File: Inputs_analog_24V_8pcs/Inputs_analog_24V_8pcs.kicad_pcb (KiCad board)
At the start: 2 copper layers, 102 parts, among them J1 Screw_Terminal_01x02, J10 Screw_Terminal_01x03, J11 Screw_Terminal_01x03, J2 Screw_Terminal_01x02, J3 Screw_Terminal_01x06, J4 Screw_Terminal_01x03, J5 Screw_Terminal_01x03, J6 Screw_Terminal_01x03, J7 Screw_Terminal_01x03, J8 Screw_Terminal_01x03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

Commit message: Update pcb
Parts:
- moved J3 132.5 mm to (152.4, 58.4), turned to 0 degrees
- moved C2 99.1 mm to (50.8, 66.0), turned to 90 degrees
- moved U3 96.8 mm to (120.7, 74.9), turned to 90 degrees
- moved U2 93.8 mm to (55.9, 67.3), turned to 90 degrees
- moved C3 89.6 mm to (116.8, 73.7), turned to 90 degrees
- moved U1 86.4 mm to (27.9, 67.3), turned to 90 degrees
- moved C1 81.5 mm to (22.9, 66.0), turned to 90 degrees
- moved C11 17.8 mm to (130.8, 121.9)
- moved C12 17.8 mm to (102.9, 121.9)
- moved C14 17.8 mm to (139.6, 96.5)
- moved C15 17.8 mm to (111.7, 96.5)
- moved C16 17.8 mm to (74.9, 121.9)
- moved C17 17.8 mm to (47.0, 121.9)
- moved C18 17.8 mm to (55.8, 96.5)
- moved C19 17.8 mm to (83.8, 96.5)
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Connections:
- U1 pad 1: input_1 -> Net-(U1-Pad1)
- U1 pad 10: GND -> Net-(U1-Pad10)
- U1 pad 11: GND -> Net-(U1-Pad11)
- U1 pad 12: GND -> Net-(U1-Pad12)
- U1 pad 13: GND -> Net-(U1-Pad13)
- U1 pad 3: input_2 -> Net-(U1-Pad3)
- U1 pad 5: input_3 -> Net-(U1-Pad5)
- U1 pad 9: input_4 -> Net-(U1-Pad9)
- U2 pad 1: input_5 -> Net-(U2-Pad1)
- U2 pad 10: GND -> Net-(U2-Pad10)
- U2 pad 11: GND -> Net-(U2-Pad11)
- U2 pad 12: GND -> Net-(U2-Pad12)
- U2 pad 13: GND -> Net-(U2-Pad13)
- U2 pad 3: input_6 -> Net-(U2-Pad3)
- U2 pad 5: input_7 -> Net-(U2-Pad5)
- U2 pad 9: input_8 -> Net-(U2-Pad9)
- U3 pad 1: Net-(U1-Pad8) -> Net-(U3-Pad1)
- U3 pad 12: Net-(U2-Pad8) -> Net-(U3-Pad12)
- U3 pad 13: Net-(U2-Pad6) -> Net-(U3-Pad13)
- U3 pad 14: Net-(U2-Pad4) -> Net-(U3-Pad14)
- U3 pad 15: Net-(U2-Pad2) -> Net-(U3-Pad15)
- U3 pad 2: Net-(U1-Pad6) -> Net-(U3-Pad2)
- U3 pad 3: Net-(U1-Pad4) -> Net-(U3-Pad3)
- U3 pad 4: Net-(U1-Pad2) -> Net-(U3-Pad4)
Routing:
- net +5V: track 490.0 -> 592.1 mm
- net GND: track 595.3 -> 671.4 mm
- net Earth: track 725.7 -> 743.5 mm
- net +24V: track 346.3 -> 364.1 mm

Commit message: Update pcb
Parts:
- added R52: 0, Resistor_THT:R_Axial_DIN0207_L6.3mm_D2.5mm_P7.62mm_Horizontal, F.Cu at (40.6, 88.9)
- added R53: 0, Resistor_THT:R_Axial_DIN0207_L6.3mm_D2.5mm_P7.62mm_Horizontal, F.Cu at (40.6, 92.7)
- moved C3 66.5 mm to (182.9, 66.0)
- moved C2 47.9 mm to (95.2, 83.8)
- moved U2 46.7 mm to (99.1, 85.1)
- moved C1 24.3 mm to (39.4, 83.8)
- moved R11 23.4 mm to (132.1, 40.6)
- moved R35 23.4 mm to (142.2, 111.8)
- moved R50 23.4 mm to (66.0, 116.8)
- moved C14 23.4 mm to (157.4, 111.8)
- moved C15 23.4 mm to (129.5, 111.8)
- moved C18 23.4 mm to (73.6, 111.8)
- moved C19 23.4 mm to (101.6, 111.8)
- moved R15 23.4 mm to (128.3, 48.3)
- moved R28 23.4 mm to (132.1, 129.5)
- moved R3 23.4 mm to (40.6, 125.7)
- moved R32 23.4 mm to (128.3, 129.5)
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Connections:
- U1 pad 1: Net-(U1-Pad1) -> input_7
- U1 pad 11: Net-(U1-Pad11) -> input_2
- U1 pad 13: Net-(U1-Pad13) -> input_1
- U1 pad 3: Net-(U1-Pad3) -> Net-(R52-Pad2)
- U1 pad 4: Net-(U1-Pad4) -> Net-(R52-Pad2)
- U1 pad 5: Net-(U1-Pad5) -> Net-(R52-Pad2)
- U1 pad 6: Net-(U1-Pad6) -> Net-(R52-Pad2)
- U1 pad 7: GND -> Net-(R53-Pad2)
- U1 pad 9: Net-(U1-Pad9) -> input_3
- U2 pad 1: Net-(U2-Pad1) -> input_8
- U2 pad 10: Net-(U2-Pad10) -> GND
- U2 pad 11: Net-(U2-Pad11) -> GND
- U2 pad 12: Net-(U2-Pad12) -> GND
- U2 pad 13: Net-(U2-Pad13) -> GND
- U2 pad 3: Net-(U2-Pad3) -> input_6
- U2 pad 5: Net-(U2-Pad5) -> input_5
- U2 pad 9: Net-(U2-Pad9) -> input_4
- U3 pad 1: Net-(U3-Pad1) -> Net-(U1-Pad8)
- U3 pad 14: Net-(U3-Pad14) -> Net-(U1-Pad12)
- U3 pad 15: Net-(U3-Pad15) -> Net-(U1-Pad10)
- U3 pad 4: Net-(U3-Pad4) -> Net-(U1-Pad2)
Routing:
- net input_3: track 14.4 -> 80.3 mm
- net input_5: track 14.4 -> 80.2 mm
- net +5V: track 592.1 -> 527.8 mm
- net input_4: track 28.3 -> 86.8 mm
- net input_7: track 14.4 -> 60.9 mm
- net input_2: track 14.4 -> 58.2 mm
- net input_6: track 14.4 -> 57.3 mm
- net input_8: track 14.3 -> 43.1 mm
- net input_1: track 14.4 -> 37.5 mm
- net Net-(U1-Pad2): track 0.00 -> 20.8 mm
- net Net-(U1-Pad12): track 0.00 -> 19.6 mm
- net Net-(R52-Pad2): track 0.00 -> 18.3 mm
- net Net-(J3-Pad4): track 0.00 -> 16.8 mm
- net Net-(R53-Pad2): track 0.00 -> 15.5 mm
- net Net-(J3-Pad1): track 0.00 -> 14.3 mm
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
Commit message: Finish pcb
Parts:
- added R54: 0, Resistor_THT:R_Axial_DIN0207_L6.3mm_D2.5mm_P7.62mm_Horizontal, F.Cu at (109.2, 86.4)
- added R55: 0, Resistor_THT:R_Axial_DIN0207_L6.3mm_D2.5mm_P7.62mm_Horizontal, F.Cu at (104.1, 86.4)
- added R56: 0, Resistor_THT:R_Axial_DIN0207_L6.3mm_D2.5mm_P7.62mm_Horizontal, F.Cu at (99.1, 86.4)
- added R57: 0, Resistor_THT:R_Axial_DIN0207_L6.3mm_D2.5mm_P7.62mm_Horizontal, F.Cu at (127.0, 85.1)
- added R58: 0, Resistor_THT:R_Axial_DIN0207_L6.3mm_D2.5mm_P7.62mm_Horizontal, F.Cu at (130.8, 94.0)
- added R59: 0, Resistor_THT:R_Axial_DIN0207_L6.3mm_D2.5mm_P7.62mm_Horizontal, F.Cu at (167.6, 94.0)
- added R60: 0, Resistor_THT:R_Axial_DIN0207_L6.3mm_D2.5mm_P7.62mm_Horizontal, F.Cu at (123.2, 94.0)
- added R61: 0, Resistor_THT:R_Axial_DIN0207_L6.3mm_D2.5mm_P7.62mm_Horizontal, F.Cu at (119.4, 94.0)
- added R62: 0, Resistor_THT:R_Axial_DIN0207_L6.3mm_D2.5mm_P7.62mm_Horizontal, F.Cu at (152.4, 88.3)
- added R63: 0, Resistor_THT:R_Axial_DIN0207_L6.3mm_D2.5mm_P7.62mm_Horizontal, F.Cu at (92.1, 69.8)
- added R64: 0, Resistor_THT:R_Axial_DIN0207_L6.3mm_D2.5mm_P7.62mm_Horizontal, F.Cu at (86.4, 69.8)
- added R65: 0, Resistor_THT:R_Axial_DIN0207_L6.3mm_D2.5mm_P7.62mm_Horizontal, F.Cu at (114.3, 94.0)
- added R66: 0, Resistor_THT:R_Axial_DIN0207_L6.3mm_D2.5mm_P7.62mm_Horizontal, F.Cu at (95.2, 86.4)
- added R67: 0, Resistor_THT:R_Axial_DIN0207_L6.3mm_D2.5mm_P7.62mm_Horizontal, F.Cu at (100.3, 97.2)
- moved C3 54.6 mm to (130.8, 82.5)
- moved C11 3.81 mm to (148.6, 133.3)
- moved C12 3.81 mm to (120.7, 133.3)
- moved C14 3.81 mm to (157.4, 108.0)
- moved C15 3.81 mm to (129.5, 108.0)
- moved C16 3.81 mm to (92.7, 133.3)
- moved C17 3.81 mm to (64.8, 133.3)
- moved C18 3.81 mm to (73.6, 108.0)
- moved C19 3.81 mm to (101.6, 108.0)
- moved J10 3.81 mm to (61.0, 133.3)
- moved J11 3.81 mm to (88.9, 133.3)
- moved J2 3.81 mm to (40.6, 133.3)
- moved J8 3.81 mm to (144.8, 133.3)
- moved J9 3.81 mm to (116.8, 133.3)
- moved R27 3.81 mm to (124.5, 133.3)
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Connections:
- C2 pad 1: GND -> Net-(C2-Pad1)
- C2 pad 2: +5V -> Net-(C2-Pad2)
- C3 pad 1: GND -> Net-(C3-Pad1)
- C3 pad 2: +5V -> Net-(C3-Pad2)
- U2 pad 1: input_8 -> Net-(R56-Pad1)
- U2 pad 14: +5V -> Net-(C2-Pad2)
- U2 pad 3: input_6 -> Net-(R55-Pad1)
- U2 pad 5: input_5 -> Net-(R54-Pad1)
- U2 pad 7: GND -> Net-(R65-Pad2)
- U3 pad 12: Net-(U3-Pad12) -> Net-(U2-Pad8)
- U3 pad 13: Net-(U3-Pad13) -> Net-(U2-Pad6)
- U3 pad 14: Net-(U1-Pad12) -> Net-(U2-Pad4)
- U3 pad 15: Net-(U1-Pad10) -> Net-(U2-Pad2)
- U3 pad 16: +5V -> Net-(C3-Pad2)
- U3 pad 2: Net-(U3-Pad2) -> Net-(U1-Pad10)
- U3 pad 3: Net-(U3-Pad3) -> Net-(U1-Pad12)
- U3 pad 8: GND -> Net-(R62-Pad1)
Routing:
- net Net-(U1-Pad2): track 20.8 -> 114.8 mm
- net Net-(U1-Pad12): track 19.6 -> 109.7 mm
- net Net-(U1-Pad10): track 13.2 -> 99.2 mm
- net Net-(U1-Pad8): track 6.88 -> 88.6 mm
- net Net-(U2-Pad2): track 0.00 -> 43.8 mm
- net GND: track 678.0 -> 721.3 mm
- net Net-(U2-Pad4): track 0.00 -> 38.8 mm
- net Net-(U2-Pad6): track 0.00 -> 36.2 mm
- net Net-(U2-Pad8): track 0.00 -> 35.9 mm
- net Net-(R60-Pad1): track 0.00 -> 31.3 mm
- net Net-(R58-Pad1): track 0.00 -> 29.2 mm
- net Net-(C3-Pad1): track 0.00 -> 25.3 mm
- net Net-(C2-Pad1): track 0.00 -> 17.0 mm
- net input_6: track 57.3 -> 43.5 mm
- net input_5: track 80.2 -> 70.9 mm
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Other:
- board outline added: 146.1 x 110.5 mm

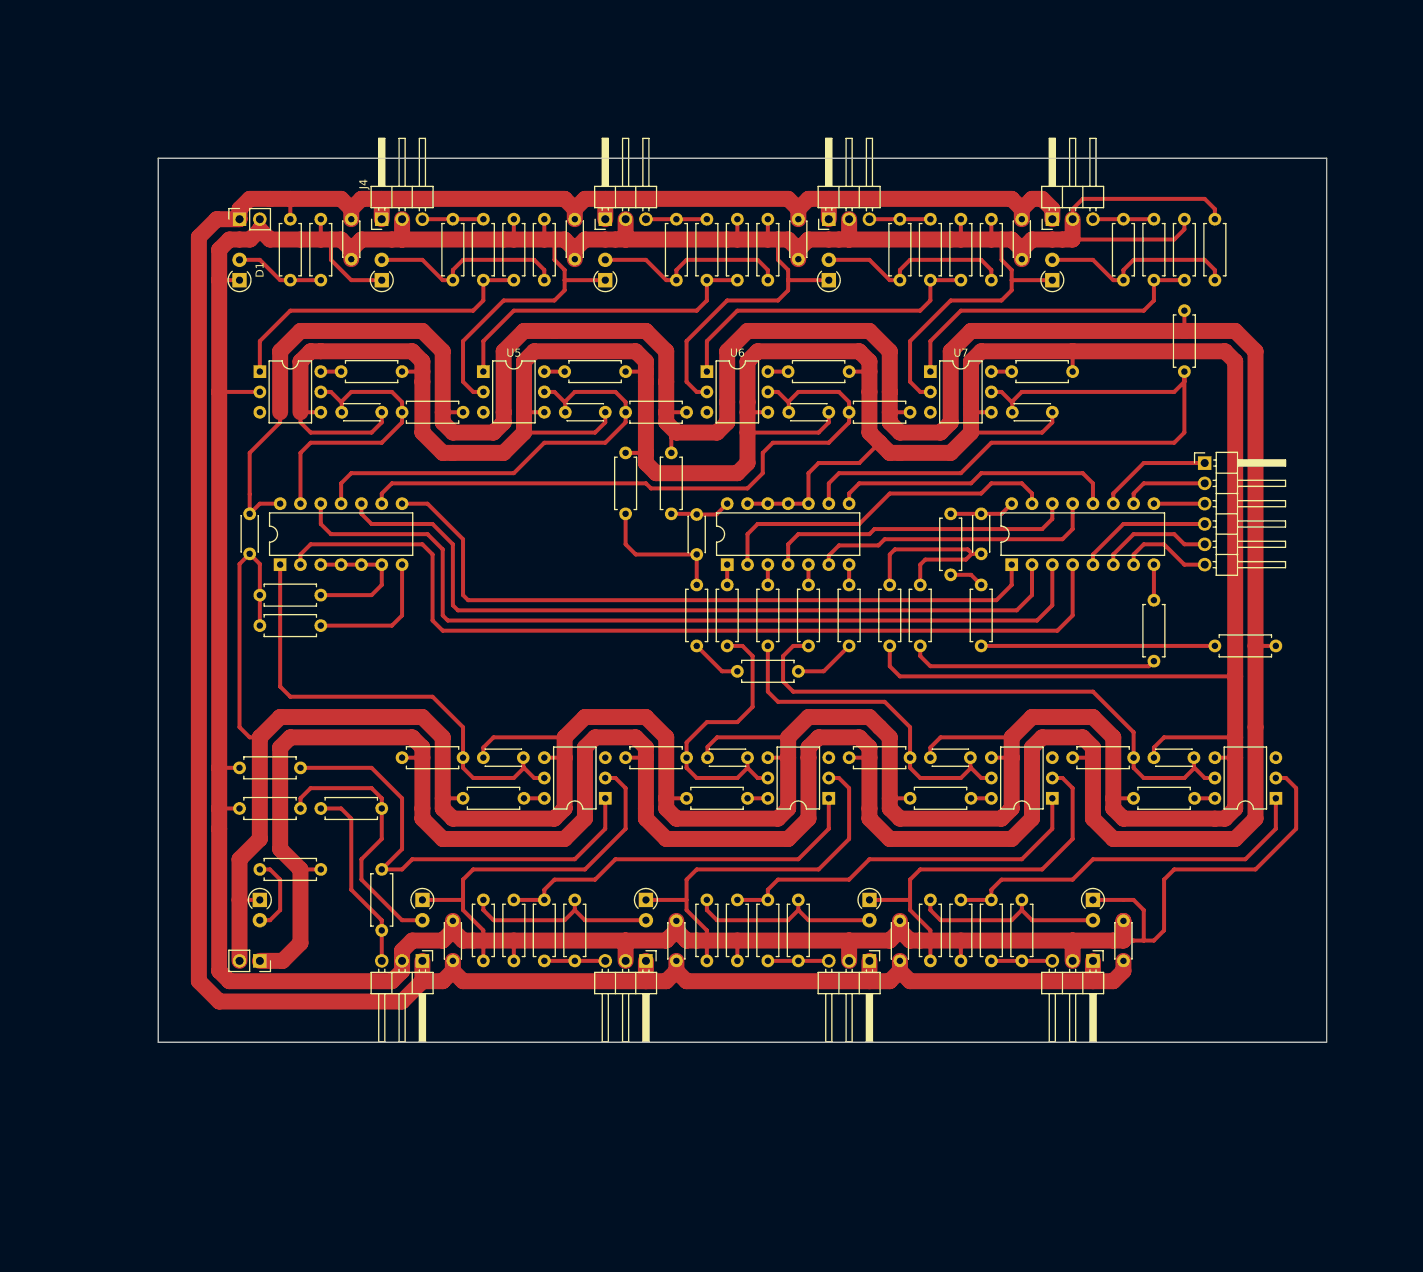
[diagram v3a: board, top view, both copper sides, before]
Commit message: Update scmematics Add pcb second layer
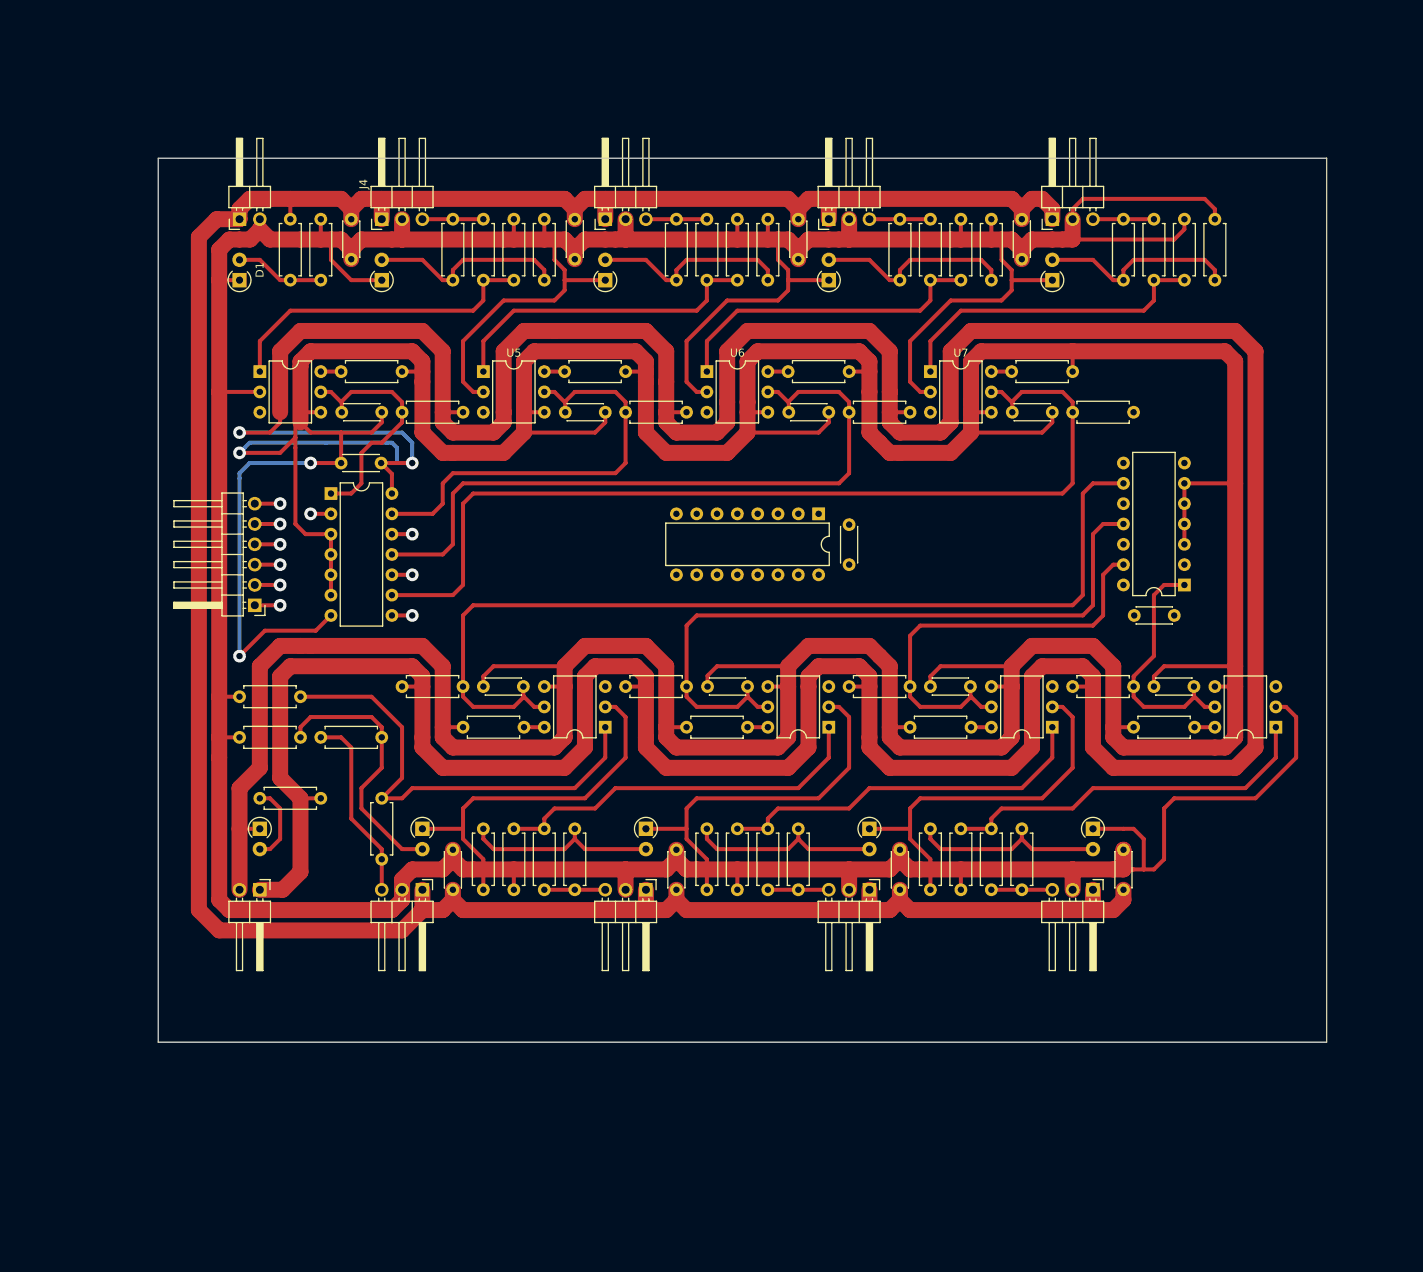
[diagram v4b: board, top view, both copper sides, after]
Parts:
- removed R52, R53, R54, R55, R56, R57, R58, R59, R60, R61, R62, R63, R64, R65, R66, R67: 0, Resistor_THT:R_Axial_DIN0207_L6.3mm_D2.5mm_P7.62mm_Horizontal
- J1, J2: footprint Connector_PinSocket_2.54mm:PinSocket_1x02_P2.54mm_Vertical -> Connector_PinHeader_2.54mm:PinHeader_1x02_P2.54mm_Horizontal
- moved J3 120.1 mm to (40.0, 88.9), turned to 180 degrees
- moved C2 60.2 mm to (154.9, 90.2), turned to 180 degrees
- moved U2 57.2 mm to (156.2, 86.4), turned to 180 degrees
- moved U3 25.0 mm to (110.5, 77.5), turned to 270 degrees
- moved C3 16.6 mm to (114.3, 83.8)
- moved C1 16.1 mm to (50.8, 71.1), turned to 0 degrees
- moved R34 14.2 mm to (149.9, 64.8), turned to 180 degrees
- moved U1 10.9 mm to (49.5, 74.9), turned to 0 degrees
- moved C11 8.89 mm to (148.6, 124.5)
- moved C12 8.89 mm to (120.7, 124.5)
- moved C14 8.89 mm to (157.4, 99.1)
- moved C15 8.89 mm to (129.5, 99.1)
- moved C16 8.89 mm to (92.7, 124.5)
- moved C17 8.89 mm to (64.8, 124.5)
- moved C18 8.89 mm to (73.6, 99.1)
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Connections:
- C2 pad 1: Net-(C2-Pad1) -> GND
- C2 pad 2: Net-(C2-Pad2) -> +5V
- C3 pad 1: Net-(C3-Pad1) -> GND
- C3 pad 2: Net-(C3-Pad2) -> +5V
- U1 pad 1: input_7 -> input_1
- U1 pad 11: input_2 -> input_3
- U1 pad 13: input_1 -> input_2
- U1 pad 3: Net-(R52-Pad2) -> GND
- U1 pad 4: Net-(R52-Pad2) -> GND
- U1 pad 5: Net-(R52-Pad2) -> GND
- U1 pad 6: Net-(R52-Pad2) -> GND
- U1 pad 7: Net-(R53-Pad2) -> GND
- U1 pad 9: input_3 -> input_4
- U2 pad 1: Net-(R56-Pad1) -> input_5
- U2 pad 10: GND -> Net-(U2-Pad10)
- U2 pad 11: GND -> input_8
- U2 pad 12: GND -> Net-(U2-Pad12)
- U2 pad 13: GND -> input_6
- U2 pad 14: Net-(C2-Pad2) -> +5V
- U2 pad 3: Net-(R55-Pad1) -> GND
- U2 pad 4: Net-(U2-Pad4) -> GND
- U2 pad 5: Net-(R54-Pad1) -> GND
- U2 pad 6: Net-(U2-Pad6) -> GND
- U2 pad 7: Net-(R65-Pad2) -> GND
- U2 pad 9: input_4 -> input_7
- U3 pad 1: Net-(U1-Pad8) -> Net-(U3-Pad1)
- U3 pad 12: Net-(U2-Pad8) -> Net-(U3-Pad12)
- U3 pad 13: Net-(U2-Pad6) -> Net-(U3-Pad13)
- U3 pad 14: Net-(U2-Pad4) -> Net-(U3-Pad14)
- U3 pad 15: Net-(U2-Pad2) -> Net-(U3-Pad15)
- U3 pad 16: Net-(C3-Pad2) -> +5V
- U3 pad 2: Net-(U1-Pad10) -> Net-(U3-Pad2)
- U3 pad 3: Net-(U1-Pad12) -> Net-(U3-Pad3)
- U3 pad 4: Net-(U1-Pad2) -> Net-(U3-Pad4)
- U3 pad 8: Net-(R62-Pad1) -> GND
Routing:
- net Net-(U1-Pad2): track 114.8 -> 2.54 mm, vias 0 -> 1
- net Net-(U1-Pad12): track 109.7 -> 2.54 mm, vias 0 -> 1
- net Net-(U1-Pad10): track 99.2 -> 2.54 mm, vias 0 -> 1
- net Net-(U1-Pad8): track 88.6 -> 2.54 mm, vias 0 -> 1
- net input_7: track 58.4 -> 120.1 mm
- net input_8: track 36.3 -> 87.0 mm
- net Net-(U2-Pad2): track 43.8 -> 0.00 mm
- net input_5: track 70.9 -> 31.2 mm
- net Net-(U2-Pad4): track 38.8 -> 0.00 mm
- net Net-(U2-Pad6): track 36.2 -> 0.00 mm
- net Net-(U2-Pad8): track 35.9 -> 0.00 mm
- net input_4: track 85.6 -> 120.1 mm
- net Net-(R60-Pad1): track 31.3 -> 0.00 mm
- net Net-(R58-Pad1): track 29.2 -> 0.00 mm
- net Net-(C3-Pad1): track 25.3 -> 0.00 mm
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
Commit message: Update pcb
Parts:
- moved C1 60.2 mm to (110.5, 78.7), turned to 270 degrees
- moved U1 57.2 mm to (106.7, 77.5), turned to 270 degrees
- moved C3 42.2 mm to (72.4, 78.7), turned to 270 degrees
- moved U3 41.9 mm to (68.6, 77.5)
- moved U2 14.5 mm to (144.8, 77.5), turned to 270 degrees
- moved C2 13.1 mm to (148.6, 78.7), turned to 270 degrees
- moved J3 1.42 mm to (39.4, 87.6)
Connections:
- U1 pad 1: input_1 -> GND
- U1 pad 11: input_3 -> input_8
- U1 pad 12: Net-(U1-Pad12) -> GND
- U1 pad 13: input_2 -> GND
- U1 pad 2: Net-(U1-Pad2) -> GND
- U1 pad 3: GND -> input_2
- U1 pad 4: GND -> Net-(U1-Pad4)
- U1 pad 5: GND -> input_1
- U1 pad 6: GND -> Net-(U1-Pad6)
- U1 pad 9: input_4 -> input_7
- U2 pad 1: input_5 -> GND
- U2 pad 11: input_8 -> input_5
- U2 pad 12: Net-(U2-Pad12) -> GND
- U2 pad 13: input_6 -> GND
- U2 pad 2: Net-(U2-Pad2) -> GND
- U2 pad 3: GND -> input_4
- U2 pad 4: GND -> Net-(U2-Pad4)
- U2 pad 5: GND -> input_3
- U2 pad 6: GND -> Net-(U2-Pad6)
- U2 pad 9: input_7 -> input_6
- U3 pad 12: Net-(U3-Pad12) -> Net-(U2-Pad10)
- U3 pad 13: Net-(U3-Pad13) -> Net-(U2-Pad8)
- U3 pad 14: Net-(U3-Pad14) -> Net-(U1-Pad10)
- U3 pad 15: Net-(U3-Pad15) -> Net-(U1-Pad8)
- U3 pad 5: Net-(J3-Pad4) -> Net-(J3-Pad6)
- U3 pad 7: Net-(J3-Pad6) -> Net-(J3-Pad4)
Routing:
- net input_4: track 120.1 -> 28.1 mm
- net Net-(U2-Pad10): track 0.00 -> 90.0 mm, vias 0 -> 2
- net Net-(U2-Pad8): track 0.00 -> 79.8 mm, vias 0 -> 2
- net input_7: track 120.1 -> 54.8 mm
- net input_8: track 87.0 -> 30.4 mm
- net input_3: track 87.1 -> 44.4 mm
- net Net-(U1-Pad10): track 2.54 -> 41.7 mm, vias 1 -> 2
- net input_1: track 30.4 -> 65.8 mm
- net GND: track 726.0 -> 758.8 mm
- net +5V: track 532.4 -> 562.3 mm
- net Net-(U1-Pad8): track 2.54 -> 30.5 mm, vias 1 -> 2
- net Net-(J3-Pad6): track 3.17 -> 26.2 mm, vias 1 -> 2
- net Net-(J3-Pad1): track 3.17 -> 23.0 mm, vias 1 -> 2
- net Net-(J3-Pad5): track 3.17 -> 23.0 mm, vias 1 -> 2
- net Net-(J3-Pad2): track 3.17 -> 20.4 mm, vias 1 -> 2
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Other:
- board size 146.1 x 110.5 mm -> 146.1 x 101.6 mm

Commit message: Redraw pcb
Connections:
- U3 pad 1: Net-(U3-Pad1) -> Net-(U1-Pad6)
- U3 pad 2: Net-(U3-Pad2) -> Net-(U1-Pad4)
- U3 pad 3: Net-(U3-Pad3) -> Net-(U2-Pad6)
- U3 pad 4: Net-(U3-Pad4) -> Net-(U2-Pad4)
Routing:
- net +5V: track 562.3 -> 675.4 mm, vias 2 -> 3
- net Net-(U2-Pad4): track 2.54 -> 92.5 mm, vias 1 -> 2
- net Net-(U2-Pad6): track 2.54 -> 82.3 mm, vias 1 -> 2
- net GND: track 758.8 -> 835.2 mm, vias 3 -> 4
- net Net-(U1-Pad4): track 2.54 -> 44.2 mm, vias 1 -> 2
- net Net-(U1-Pad6): track 2.54 -> 34.1 mm, vias 1 -> 2
- net Net-(U3-Pad4): track 2.54 -> 0.00 mm, vias 1 -> 0
- net Net-(U3-Pad3): track 2.54 -> 0.00 mm, vias 1 -> 0
- net Net-(U3-Pad2): track 2.54 -> 0.00 mm, vias 1 -> 0
- net Net-(U3-Pad1): track 2.54 -> 0.00 mm, vias 1 -> 0

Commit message: Update Inputs pcb
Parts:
- D1, D10, D2, D3, D4, D5, D6, D7, D8, D9: footprint Diode_THT:D_A-405_P2.54mm_Vertical_AnodeUp -> LED_THT:LED_D3.0mm
- J1, J2: footprint Connector_PinHeader_2.54mm:PinHeader_1x02_P2.54mm_Horizontal -> Connector_PinHeader_2.54mm:PinHeader_1x02_P2.54mm_Vertical
- J10, J11, J4, J5, J6, J7, J8, J9: footprint Connector_PinHeader_2.54mm:PinHeader_1x03_P2.54mm_Horizontal -> Connector_PinHeader_2.54mm:PinHeader_1x03_P2.54mm_Vertical
- J3: footprint Connector_PinHeader_2.54mm:PinHeader_1x06_P2.54mm_Horizontal -> Connector_PinHeader_2.54mm:PinHeader_1x06_P2.54mm_Vertical
